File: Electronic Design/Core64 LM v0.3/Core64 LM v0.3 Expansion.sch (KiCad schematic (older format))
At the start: 14 parts, among them J3 Conn_01x01_Male, J4 Conn_01x01_Male, J5 Conn_01x01_Male, J6 Conn_01x01_Male

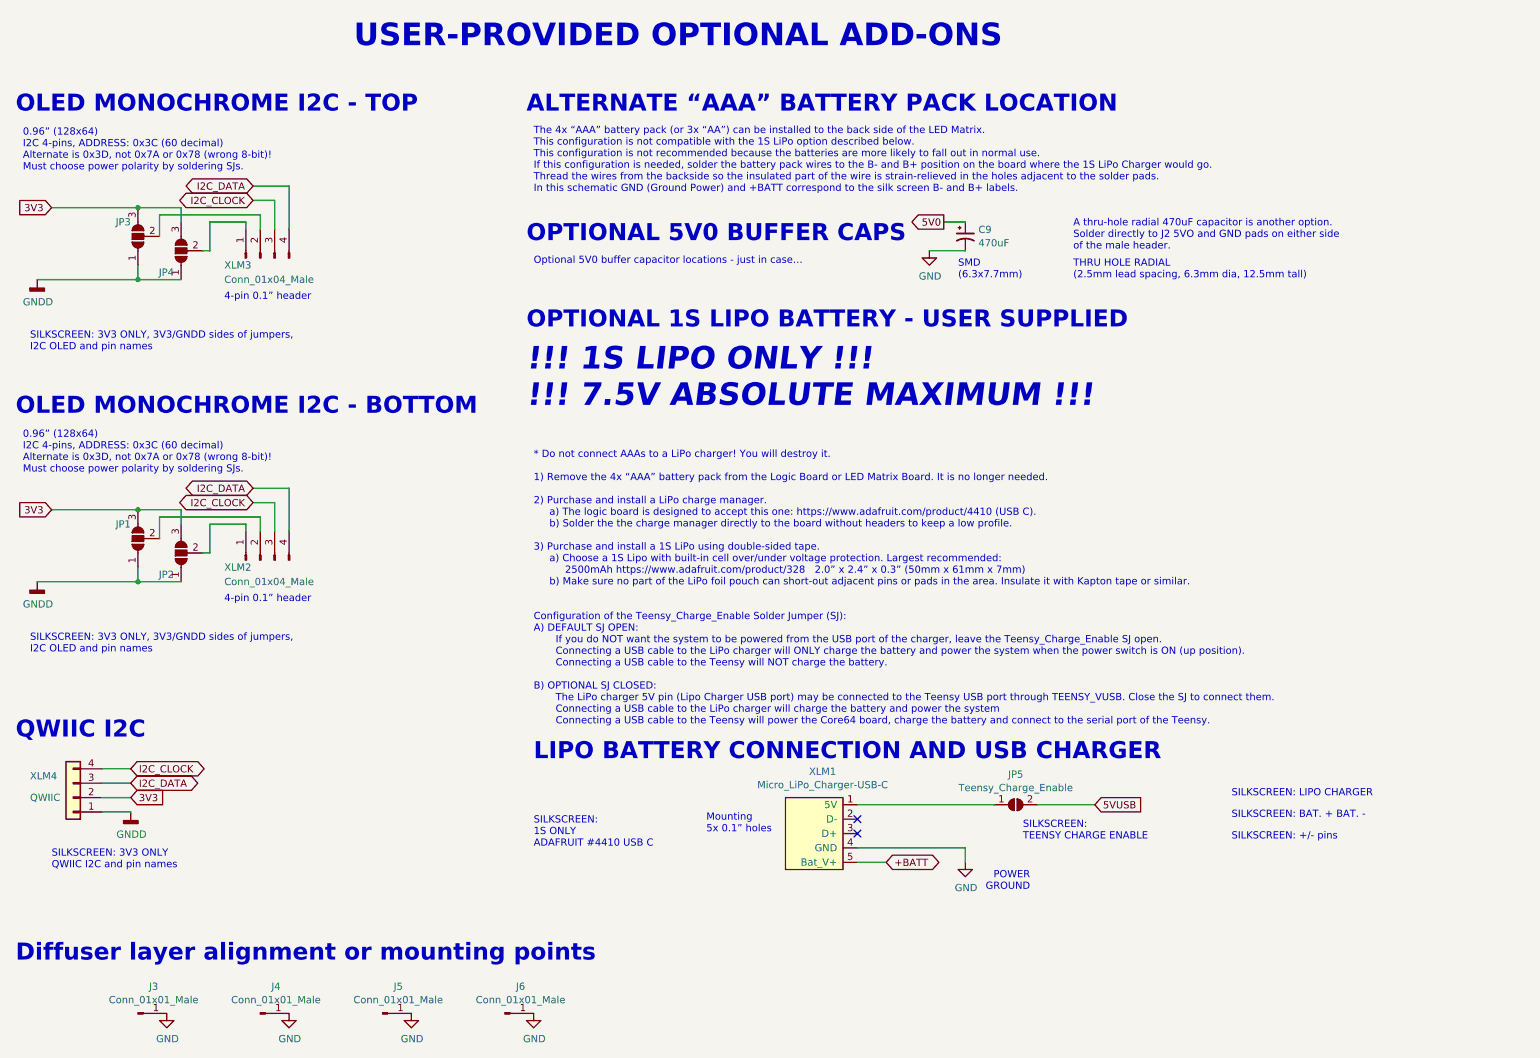
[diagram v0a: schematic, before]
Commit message: Add opt. 5V0 buffer cap SMD and T.H., add PCB P/N, move corner holes to 37.7mm, move diffuser alignment mount points out and disconnect from GND, silkscreen cleanup
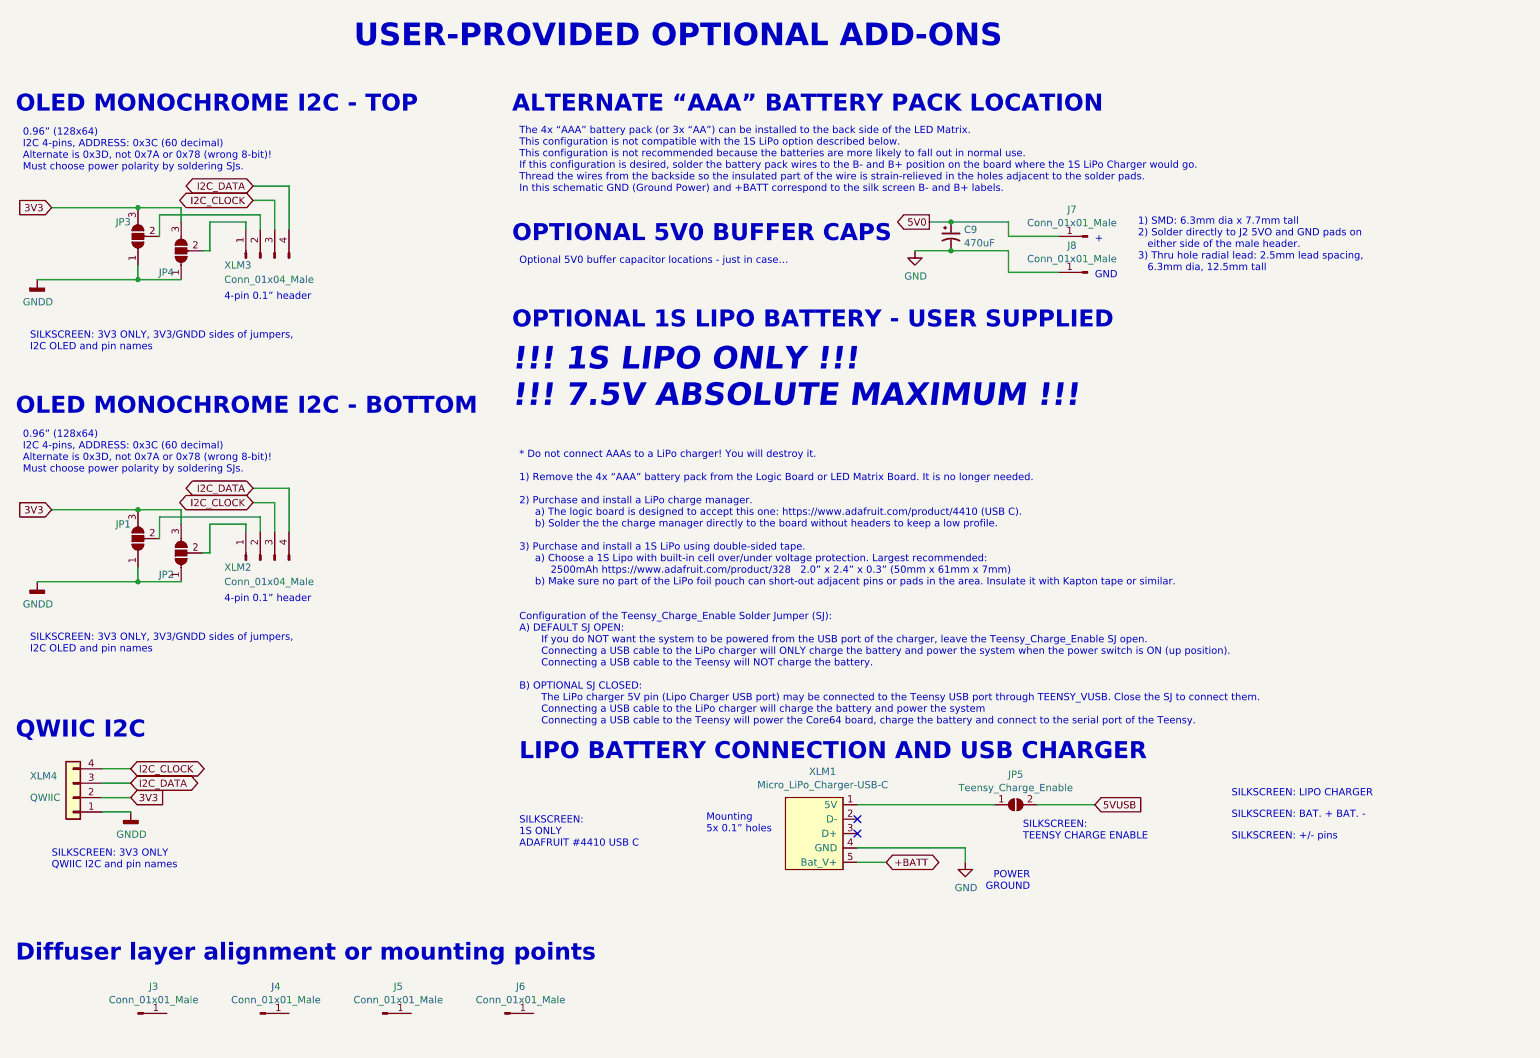
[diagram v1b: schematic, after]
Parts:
- added J7, J8: Conn_01x01_Male, Connector_PinHeader_2.54mm:PinHeader_1x01_P2.54mm_Vertical_No_Registration, symbol Connector:Conn_01x01_Male
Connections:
- net 5V0: now also J7.1 (Pin_1)
- net GND: now also J8.1 (Pin_1); no longer J3.1 (Pin_1), J4.1 (Pin_1), J5.1 (Pin_1), J6.1 (Pin_1)
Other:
- note added: "+"
- note added: "1) SMD: 6.3mm dia x 7.7mm tall\n2) Solder directly to J2 5VO and GND pads on\n either side of the male header.\n3) Thru hole radial lead: 2.5mm lead spacing, \n 6.3mm dia, 12.5mm tall"
- note added: "GND"
- note added: "The 4x “AAA” battery pack (or 3x “AA”) can be installed to the back side of the LED Matrix.\nThis configuration is not compatible with the 1S LiPo option described below.\nThis configuration is not recommended because the batteries are more likely to fall out in normal use.\nIf this configuration is desired, solder the battery pack wires to the B- and B+ position on the board where the 1S LiPo Ch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"
- note removed: "A thru-hole radial 470uF capacitor is another option.\nSolder directly to J2 5VO and GND pads on either side\nof the male header."
- note removed: "SMD\n(6.3x7.7mm)"
- note removed: "THRU HOLE RADIAL\n(2.5mm lead spacing, 6.3mm dia, 12.5mm tall)"
- note removed: "The 4x “AAA” battery pack (or 3x “AA”) can be installed to the back side of the LED Matrix.\nThis configuration is not compatible with the 1S LiPo option described below.\nThis configuration is not recommended because the batteries are more likely to fall out in normal use.\nIf this configuration is needed, solder the battery pack wires to the B- and B+ position on the board where the 1S LiPo Cha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"
- moved on the sheet: C9
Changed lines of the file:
@@
 Sheet 2 2
 Title "Core64 LM (LED MATRIX)"
-Date "2021-05-17"
+Date "2021-08-07"
 Rev "0.3"
 Comp "Concept and design by Andy Geppert @ www.MachineIdeas.com"
@@
 	1    0    0    -1
 $EndComp
-Text Notes 4400 5800 0    118  ~ 24
+Text Notes 4300 5800 0    118  ~ 24
 LIPO BATTERY CONNECTION AND USB CHARGER
 Text Notes 3150 850  0    157  ~ 31
@@
 Wire Wire Line
 	7400 6400 7400 6500
-Text Notes 4400 6400 0    50   ~ 0
+Text Notes 4300 6400 0    50   ~ 0
 SILKSCREEN:\n1S ONLY\nADAFRUIT #4410 USB C
 $Comp
@@
 Wire Wire Line
 	7900 6100 8300 6100
-Text Notes 4350 2800 0    118  ~ 24
+Text Notes 4250 2800 0    118  ~ 24
 OPTIONAL 1S LIPO BATTERY - USER SUPPLIED
-Text Notes 4350 3350 0    157  Italic 31
+Text Notes 4250 3350 0    157  Italic 31
 !!! 1S LIPO ONLY !!!\n!!! 7.5V ABSOLUTE MAXIMUM !!!
 Text Notes 9250 6350 0    50   ~ 0
@@
 Text Notes 5600 6300 0    50   ~ 0
 Mounting\n5x 0.1” holes
-Text Notes 4400 5550 0    50   ~ 0
+Text Notes 4300 5550 0    50   ~ 0
 * Do not connect AAAs to a LiPo charger! You will destroy it.\n\n1) Remove the 4x “AAA” battery pack from the Logic Board or LED Matrix Board. It is no longer needed.\n\n2) Purchase and install a LiPo charge manager.\n     a) The logic board is designed to accept this one: https://www.adafruit.com/product/4410 (USB C).\n     b) Solder the the charge manager directly to the board without headers to keep a low profile.\n\n3) Purchase and install a 1S LiPo using double-sided tape. \n     a) Choose a 1S Lipo with built-in cell over/under voltage protection. Largest recommended:\n          2500mAh https://www.adafruit.com/product/328   2.0” x 2.4” x 0.3” (50mm x 61mm x 7mm)\n     b) Make sure no part of the LiPo foil pouch can short-out adjacent pins or pads in the area. Insulate it with Kapton tape or similar.\n\n\nConfiguration of the Teensy_Charge_Enable Solder Jumper (SJ):\nA) DEFAULT SJ OPEN:\n       If you do NOT want the system to be powered from the USB port of the charger, leave the Teensy_Charge_Enable SJ open.\n       Connecting a USB cable to the LiPo charger will ONLY charge the battery and power the system when the power switch is ON (up position).\n       Connecting a USB cable to the Teensy will NOT charge the battery.\n\nB) OPTIONAL SJ CLOSED:\n       The LiPo charger 5V pin (Lipo Charger USB port) may be connected to the Teensy USB port through TEENSY_VUSB. Close the SJ to connect them.\n       Connecting a USB cable to the LiPo charger will charge the battery and power the system \n       Connecting a USB cable to the Teensy will power the Core64 board, charge the battery and connect to the serial port of the Teensy.\n
 Text Notes 800  3400 0    118  ~ 24
@@
 	1    0    0    -1
 $EndComp
-$Comp
-L power:GND #PWR?
-U 1 1 607ECE86
-P 1850 7550
-AR Path="/607ECE86" Ref="#PWR?"  Part="1"
-AR Path="/603A0E05/607ECE86" Ref="#PWR0111"  Part="1"
-F 0 "#PWR0111" H 1850 7300 50  0001 C CNN
-F 1 "GND" H 1855 7373 50  0000 C CNN
-F 2 "" H 1850 7550 50  0001 C CNN
-F 3 "" H 1850 7550 50  0001 C CNN
-	1    1850 7550
-	1    0    0    -1
-$EndComp
-$Comp
-L power:GND #PWR?
-U 1 1 607EDA9C
-P 2700 7550
-AR Path="/607EDA9C" Ref="#PWR?"  Part="1"
-AR Path="/603A0E05/607EDA9C" Ref="#PWR0112"  Part="1"
-F 0 "#PWR0112" H 2700 7300 50  0001 C CNN
-F 1 "GND" H 2705 7373 50  0000 C CNN
-F 2 "" H 2700 7550 50  0001 C CNN
-F 3 "" H 2700 7550 50  0001 C CNN
-	1    2700 7550
-	1    0    0    -1
-$EndComp
-$Comp
-L power:GND #PWR?
-U 1 1 607EE7C2
-P 3550 7550
-AR Path="/607EE7C2" Ref="#PWR?"  Part="1"
-AR Path="/603A0E05/607EE7C2" Ref="#PWR0113"  Part="1"
-F 0 "#PWR0113" H 3550 7300 50  0001 C CNN
-F 1 "GND" H 3555 7373 50  0000 C CNN
-F 2 "" H 3550 7550 50  0001 C CNN
-F 3 "" H 3550 7550 50  0001 C CNN
-	1    3550 7550
-	1    0    0    -1
-$EndComp
-$Comp
-L power:GND #PWR?
-U 1 1 607EF44F
-P 4400 7550
-AR Path="/607EF44F" Ref="#PWR?"  Part="1"
-AR Path="/603A0E05/607EF44F" Ref="#PWR0114"  Part="1"
-F 0 "#PWR0114" H 4400 7300 50  0001 C CNN
-F 1 "GND" H 4405 7373 50  0000 C CNN
-F 2 "" H 4400 7550 50  0001 C CNN
-F 3 "" H 4400 7550 50  0001 C CNN
-	1    4400 7550
-	1    0    0    -1
-$EndComp
 Text Notes 7800 6350 0    50   ~ 0
 SILKSCREEN:\nTEENSY CHARGE ENABLE
 Text Notes 800  7200 0    118  ~ 24
 Diffuser layer alignment or mounting points
-Text Notes 4350 1300 0    118  ~ 24
+Text Notes 4250 1300 0    118  ~ 24
 ALTERNATE “AAA” BATTERY PACK LOCATION
-Text Notes 4400 1850 0    50   ~ 0
-The 4x “AAA” battery pack (or 3x “AA”) can be installed to the back side of the LED Matrix.\nThis configuration is not compatible with the 1S LiPo option described below.\nThis configuration is not recommended because the batteries are more likely to fall out in normal use.\nIf this configuration is needed, solder the battery pack wires to the B- and B+ position on the board where the 1S LiPo Charger would go. \nThread the wires from the backside so the insulated part of the wire is strain-relieved in the holes adjacent to the solder pads.\nIn this schematic GND (Ground Power) and +BATT correspond to the silk screen B- and B+ labels.
+Text Notes 4300 1850 0    50   ~ 0
+The 4x “AAA” battery pack (or 3x “AA”) can be installed to the back side of the LED Matrix.\nThis configuration is not compatible with the 1S LiPo option described below.\nThis configuration is not recommended because the batteries are more likely to fall out in normal use.\nIf this configuration is desired, solder the battery pack wires to the B- and B+ position on the board where the 1S LiPo Charger would go. \nThread the wires from the backside so the insulated part of the wire is strain-relieved in the holes adjacent to the solder pads.\nIn this schematic GND (Ground Power) and +BATT correspond to the silk screen B- and B+ labels.
 $Comp
 L power:GND #PWR?
 U 1 1 60AC7B04
-P 7150 2250
+P 7050 2250
 AR Path="/60AC7B04" Ref="#PWR?"  Part="1"
 AR Path="/603A0E05/60AC7B04" Ref="#PWR0115"  Part="1"
-F 0 "#PWR0115" H 7150 2000 50  0001 C CNN
-F 1 "GND" H 7155 2073 50  0000 C CNN
-F 2 "" H 7150 2250 50  0001 C CNN
-F 3 "" H 7150 2250 50  0001 C CNN
-	1    7150 2250
-	1    0    0    -1
-$EndComp
-Text GLabel 7250 2050 0    50   Output ~ 0
+F 0 "#PWR0115" H 7050 2000 50  0001 C CNN
+F 1 "GND" H 7055 2073 50  0000 C CNN
+F 2 "" H 7050 2250 50  0001 C CNN
+F 3 "" H 7050 2250 50  0001 C CNN
+	1    7050 2250
+	1    0    0    -1
+$EndComp
+Text GLabel 7150 2050 0    50   Output ~ 0
 5V0
-Text Notes 4350 2200 0    118  ~ 24
+Text Notes 4250 2200 0    118  ~ 24
 OPTIONAL 5V0 BUFFER CAPS
-Text Notes 4400 2350 0    50   ~ 0
+Text Notes 4300 2350 0    50   ~ 0
 Optional 5V0 buffer capacitor locations - just in case…
 $Comp
 L Device:CP1_Small C9
 U 1 1 60AD3B01
-P 7400 2150
-F 0 "C9" H 7491 2197 50  0000 L CNN
-F 1 "470uF" H 7491 2104 50  0000 L CNN
-F 2 "Capacitor_SMD:CP_Elec_6.3x7.7" H 7400 2150 50  0001 C CNN
-F 3 "~" H 7400 2150 50  0001 C CNN
-	1    7400 2150
-	1    0    0    -1
-$EndComp
-Wire Wire Line
-	7150 2250 7400 2250
-Wire Wire Line
-	7250 2050 7400 2050
-Text Notes 7350 2450 0    50   ~ 0
-SMD\n(6.3x7.7mm)
-Text Notes 8150 2450 0    50   ~ 0
-THRU HOLE RADIAL\n(2.5mm lead spacing, 6.3mm dia, 12.5mm tall)
-Text Notes 8150 2250 0    50   ~ 0
-A thru-hole radial 470uF capacitor is another option.\nSolder directly to J2 5VO and GND pads on either side\nof the male header.
+P 7300 2150
+F 0 "C9" H 7391 2197 50  0000 L CNN
+F 1 "470uF" H 7391 2104 50  0000 L CNN
+F 2 "Capacitor_SMD:CP_Elec_6.3x7.7" H 7300 2150 50  0001 C CNN
+F 3 "~" H 7300 2150 50  0001 C CNN
+	1    7300 2150
+	1    0    0    -1
+$EndComp
+Wire Wire Line
+	7050 2250 7300 2250
+Wire Wire Line
+	7150 2050 7300 2050
+Text Notes 8600 2400 0    50   ~ 0
+1) SMD: 6.3mm dia x 7.7mm tall\n2) Solder directly to J2 5VO and GND pads on\n   either side of the male header.\n3) Thru hole radial lead: 2.5mm lead spacing, \n   6.3mm dia, 12.5mm tall
+$Comp
+L Connector:Conn_01x01_Male J7
+U 1 1 61180BD1
+P 8250 2150
+F 0 "J7" H 8359 2337 50  0000 C CNN
+F 1 "Conn_01x01_Male" H 8359 2244 50  0000 C CNN
+F 2 "Connector_PinHeader_2.54mm:PinHeader_1x01_P2.54mm_Vertical_No_Registration" H 8250 2150 50  0001 C CNN
+F 3 "~" H 8250 2150 50  0001 C CNN
+	1    8250 2150
+	-1   0    0    -1
+$EndComp
+$Comp
+L Connector:Conn_01x01_Male J8
+U 1 1 61180BD7
+P 8250 2400
+F 0 "J8" H 8359 2587 50  0000 C CNN
+F 1 "Conn_01x01_Male" H 8359 2494 50  0000 C CNN
+F 2 "Connector_PinHeader_2.54mm:PinHeader_1x01_P2.54mm_Vertical_No_Registration" H 8250 2400 50  0001 C CNN
+F 3 "~" H 8250 2400 50  0001 C CNN
+	1    8250 2400
+	-1   0    0    -1
+$EndComp
+Wire Wire Line
+	7300 2050 7700 2050
+Wire Wire Line
+	7700 2050 7700 2150
+Wire Wire Line
+	7700 2150 8050 2150
+Connection ~ 7300 2050
+Wire Wire Line
+	7300 2250 7700 2250
+Wire Wire Line
+	7700 2250 7700 2400
+Wire Wire Line
+	7700 2400 8050 2400
+Connection ~ 7300 2250
+Text Notes 8300 2200 0    50   ~ 0
++
+Text Notes 8300 2450 0    50   ~ 0
+GND
 $EndSCHEMATC

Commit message: Core64 LED Matrix V0.3 release to manufacturing
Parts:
- C9, J3, J4, J5, J6, J7, J8, JP1, JP2, JP3, JP4, JP5, XLM1, XLM2, XLM3, XLM4: INSERT? (none) -> NO
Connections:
- no-connect marks 2 -> 6
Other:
- note added: "DNI"
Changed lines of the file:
@@
 encoding utf-8
 Sheet 2 2
-Title "Core64 LM (LED MATRIX)"
-Date "2021-08-07"
+Title "Core64 LED MATRIX (LM)"
+Date "2021-10-02"
 Rev "0.3"
-Comp "Concept and design by Andy Geppert @ www.MachineIdeas.com"
+Comp "Concept and design by Andy Geppert | www.MachineIdeas.com"
 Comment1 "Visit www.Core64.io for information on assembly and optional features."
-Comment2 "*** WIP ***"
+Comment2 "As released 2021-10-02"
 Comment3 ""
 Comment4 "All capacitors ceramic X7R unless otherwise noted."
@@
 F 2 "Jumper:SolderJumper-3_P1.3mm_Open_Pad1.0x1.5mm_NumberLabels" H 1950 4350 50  0001 C CNN
 F 3 "~" H 1950 4350 50  0001 C CNN
+F 4 "NO" H 1950 4350 50  0001 C CNN "INSERT?"
 	1    1950 4350
 	0    -1   -1   0
@@
 F 2 "Jumper:SolderJumper-3_P1.3mm_Open_Pad1.0x1.5mm_NumberLabels" H 1650 4250 50  0001 C CNN
 F 3 "~" H 1650 4250 50  0001 C CNN
+F 4 "NO" H 1650 4250 50  0001 C CNN "INSERT?"
 	1    1650 4250
 	0    -1   -1   0
@@
 F 2 "Connector_JST:JST_SH_SM04B-SRSS-TB_1x04-1MP_P1.00mm_Horizontal" H 1200 6050 50  0001 C CNN
 F 3 "~" H 1200 6050 50  0001 C CNN
+F 4 "NO" H 1200 6050 50  0001 C CNN "INSERT?"
 	1    1200 6050
 	-1   0    0    1
@@
 F 2 "Connector_PinHeader_2.54mm:PinHeader_1x04_P2.54mm_Vertical" H 2500 4400 50  0001 C CNN
 F 3 "~" H 2500 4400 50  0001 C CNN
+F 4 "NO" H 2500 4400 50  0001 C CNN "INSERT?"
 	1    2500 4400
 	0    -1   -1   0
@@
 F 2 "Jumper:SolderJumper-2_P1.3mm_Open_Pad1.0x1.5mm" H 7750 6100 50  0001 C CNN
 F 3 "~" H 7750 6100 50  0001 C CNN
+F 4 "NO" H 7750 6100 50  0001 C CNN "INSERT?"
 	1    7750 6100
 	1    0    0    -1
@@
 F 2 "Jumper:SolderJumper-3_P1.3mm_Open_Pad1.0x1.5mm_NumberLabels" H 1950 2250 50  0001 C CNN
 F 3 "~" H 1950 2250 50  0001 C CNN
+F 4 "NO" H 1950 2250 50  0001 C CNN "INSERT?"
 	1    1950 2250
 	0    -1   -1   0
@@
 F 2 "Jumper:SolderJumper-3_P1.3mm_Open_Pad1.0x1.5mm_NumberLabels" H 1650 2150 50  0001 C CNN
 F 3 "~" H 1650 2150 50  0001 C CNN
+F 4 "NO" H 1650 2150 50  0001 C CNN "INSERT?"
 	1    1650 2150
 	0    -1   -1   0
@@
 F 2 "Connector_PinHeader_2.54mm:PinHeader_1x04_P2.54mm_Vertical" H 2500 2300 50  0001 C CNN
 F 3 "~" H 2500 2300 50  0001 C CNN
+F 4 "NO" H 2500 2300 50  0001 C CNN "INSERT?"
 	1    2500 2300
 	0    -1   -1   0
@@
 F 2 "Core_Memory_8x8_Array:Micro_LiPo_Charger_USB-C_CornerSMD" H 6350 6200 50  0001 C CNN
 F 3 "" H 6350 6200 50  0001 C CNN
+F 4 "NO" H 6350 6200 50  0001 C CNN "INSERT?"
 	1    6350 6200
 	1    0    0    -1
@@
 F 2 "Connector_PinHeader_2.54mm:PinHeader_1x01_P2.54mm_Vertical_No_Registration" H 4200 7550 50  0001 C CNN
 F 3 "~" H 4200 7550 50  0001 C CNN
+F 4 "NO" H 4200 7550 50  0001 C CNN "INSERT?"
 	1    4200 7550
 	1    0    0    -1
@@
 F 2 "Connector_PinHeader_2.54mm:PinHeader_1x01_P2.54mm_Vertical_No_Registration" H 2500 7550 50  0001 C CNN
 F 3 "~" H 2500 7550 50  0001 C CNN
+F 4 "NO" H 2500 7550 50  0001 C CNN "INSERT?"
 	1    2500 7550
 	1    0    0    -1
@@
 F 2 "Connector_PinHeader_2.54mm:PinHeader_1x01_P2.54mm_Vertical_No_Registration" H 1650 7550 50  0001 C CNN
 F 3 "~" H 1650 7550 50  0001 C CNN
+F 4 "NO" H 1650 7550 50  0001 C CNN "INSERT?"
 	1    1650 7550
 	1    0    0    -1
@@
 F 2 "Connector_PinHeader_2.54mm:PinHeader_1x01_P2.54mm_Vertical_No_Registration" H 3350 7550 50  0001 C CNN
 F 3 "~" H 3350 7550 50  0001 C CNN
+F 4 "NO" H 3350 7550 50  0001 C CNN "INSERT?"
 	1    3350 7550
 	1    0    0    -1
@@
 F 2 "Capacitor_SMD:CP_Elec_6.3x7.7" H 7300 2150 50  0001 C CNN
 F 3 "~" H 7300 2150 50  0001 C CNN
+F 4 "NO" H 7300 2150 50  0001 C CNN "INSERT?"
 	1    7300 2150
 	1    0    0    -1
@@
 F 2 "Connector_PinHeader_2.54mm:PinHeader_1x01_P2.54mm_Vertical_No_Registration" H 8250 2150 50  0001 C CNN
 F 3 "~" H 8250 2150 50  0001 C CNN
+F 4 "NO" H 8250 2150 50  0001 C CNN "INSERT?"
 	1    8250 2150
 	-1   0    0    -1
@@
 F 2 "Connector_PinHeader_2.54mm:PinHeader_1x01_P2.54mm_Vertical_No_Registration" H 8250 2400 50  0001 C CNN
 F 3 "~" H 8250 2400 50  0001 C CNN
+F 4 "NO" H 8250 2400 50  0001 C CNN "INSERT?"
 	1    8250 2400
 	-1   0    0    -1
@@
 Text Notes 8300 2450 0    50   ~ 0
 GND
+Text Notes 7400 2050 0    50   ~ 0
+DNI
+Text Notes 7900 2250 0    50   ~ 0
+DNI
+Text Notes 7900 2000 0    50   ~ 0
+DNI
+Text Notes 1700 7700 0    50   ~ 0
+DNI
+Text Notes 2550 7700 0    50   ~ 0
+DNI
+Text Notes 3400 7700 0    50   ~ 0
+DNI
+Text Notes 4250 7700 0    50   ~ 0
+DNI
+NoConn ~ 4400 7550
+NoConn ~ 3550 7550
+NoConn ~ 2700 7550
+NoConn ~ 1850 7550
 $EndSCHEMATC
